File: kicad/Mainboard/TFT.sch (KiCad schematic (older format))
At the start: 3 parts, among them J7 Conn_01x10, Q2 BSS138

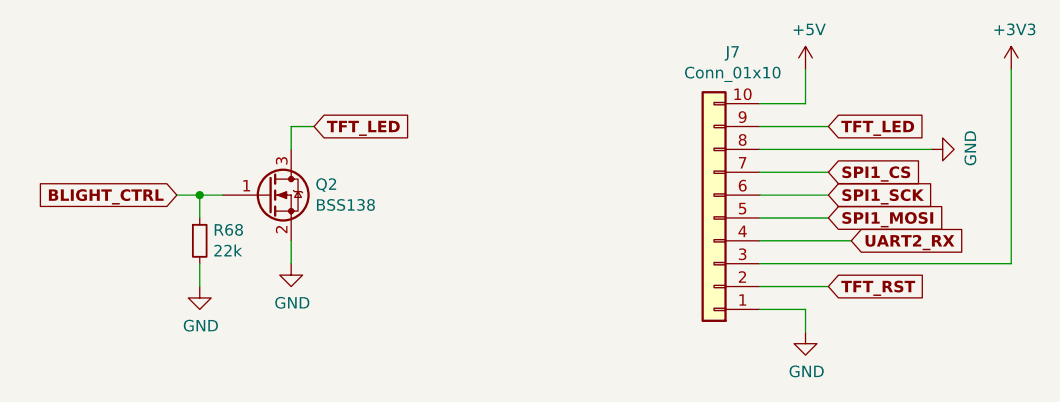
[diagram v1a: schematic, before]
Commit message: UART3 swapped with UART2 - now keyboard  uses UART3, and WIFI uses UART2; added ladder for ADF7021 data lines; further pcb improvement(shielding for ADF7021 part)
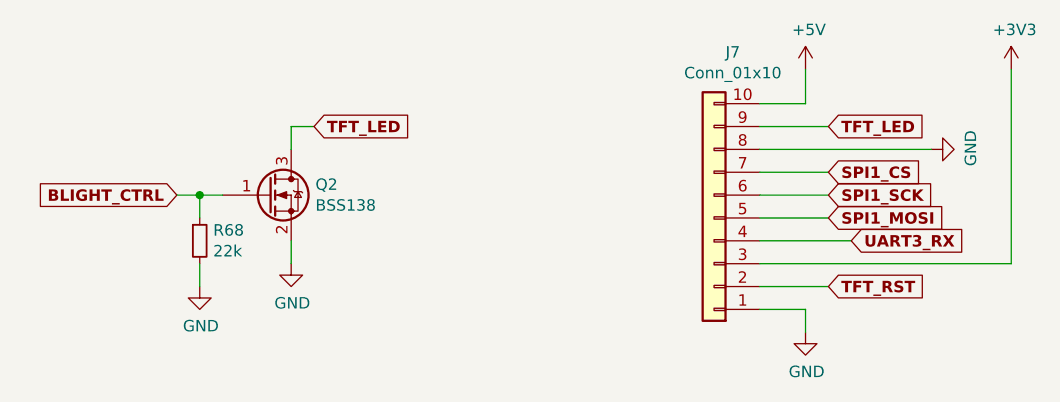
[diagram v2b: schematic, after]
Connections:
- net UART2_RX renamed UART3_RX
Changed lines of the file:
@@
 	6450 4150 6750 4150
 Text GLabel 6850 3950 2    50   Input ~ 10
-UART2_RX
+UART3_RX
 Wire Wire Line
 	6450 3950 6850 3950

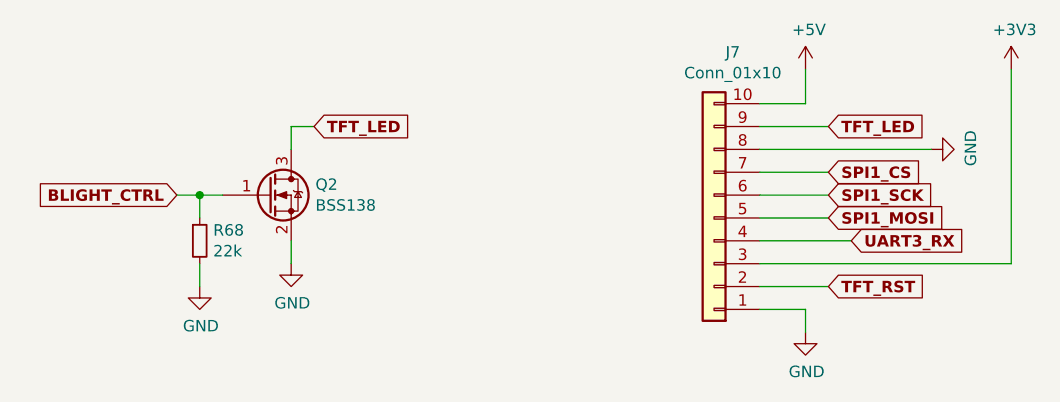
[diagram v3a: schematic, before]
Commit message: added 6 testpoints
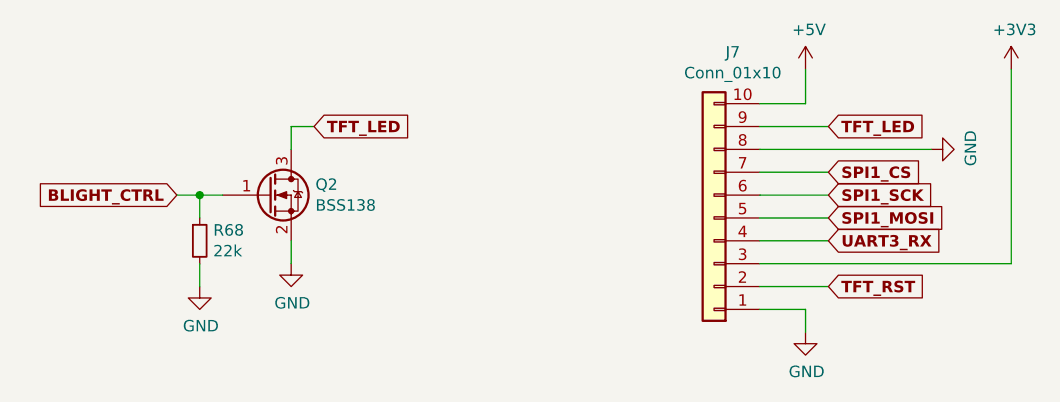
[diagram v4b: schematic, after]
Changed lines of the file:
@@
 EESchema Schematic File Version 4
-LIBS:Mainboard-cache
 EELAYER 30 0
 EELAYER END
@@
 Wire Wire Line
 	6450 4150 6750 4150
-Text GLabel 6850 3950 2    50   Input ~ 10
+Text GLabel 6750 3950 2    50   Input ~ 10
 UART3_RX
-Wire Wire Line
-	6450 3950 6850 3950
 $Comp
 L Mainboard-rescue:Conn_01x10-Connector_Generic J7
@@
 	3900 3750 4000 3750
 Connection ~ 4000 3750
+Wire Wire Line
+	6450 3950 6750 3950
 $EndSCHEMATC
